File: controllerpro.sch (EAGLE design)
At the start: 11 parts

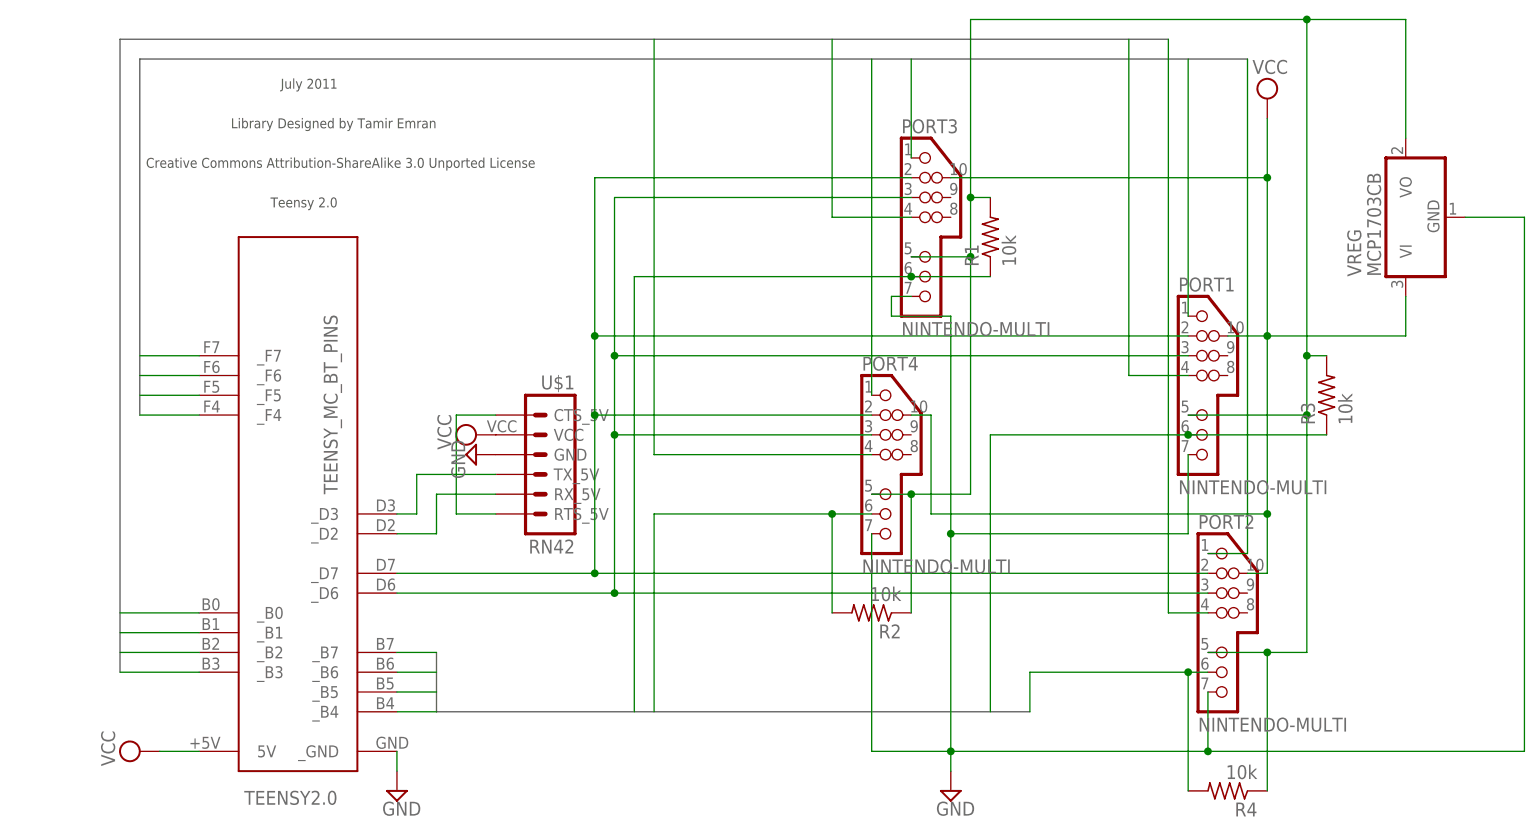
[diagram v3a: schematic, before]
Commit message: Switch VCC to 3.3v
Remove VREG, supply NES/SNES and N64 all with 3.3v
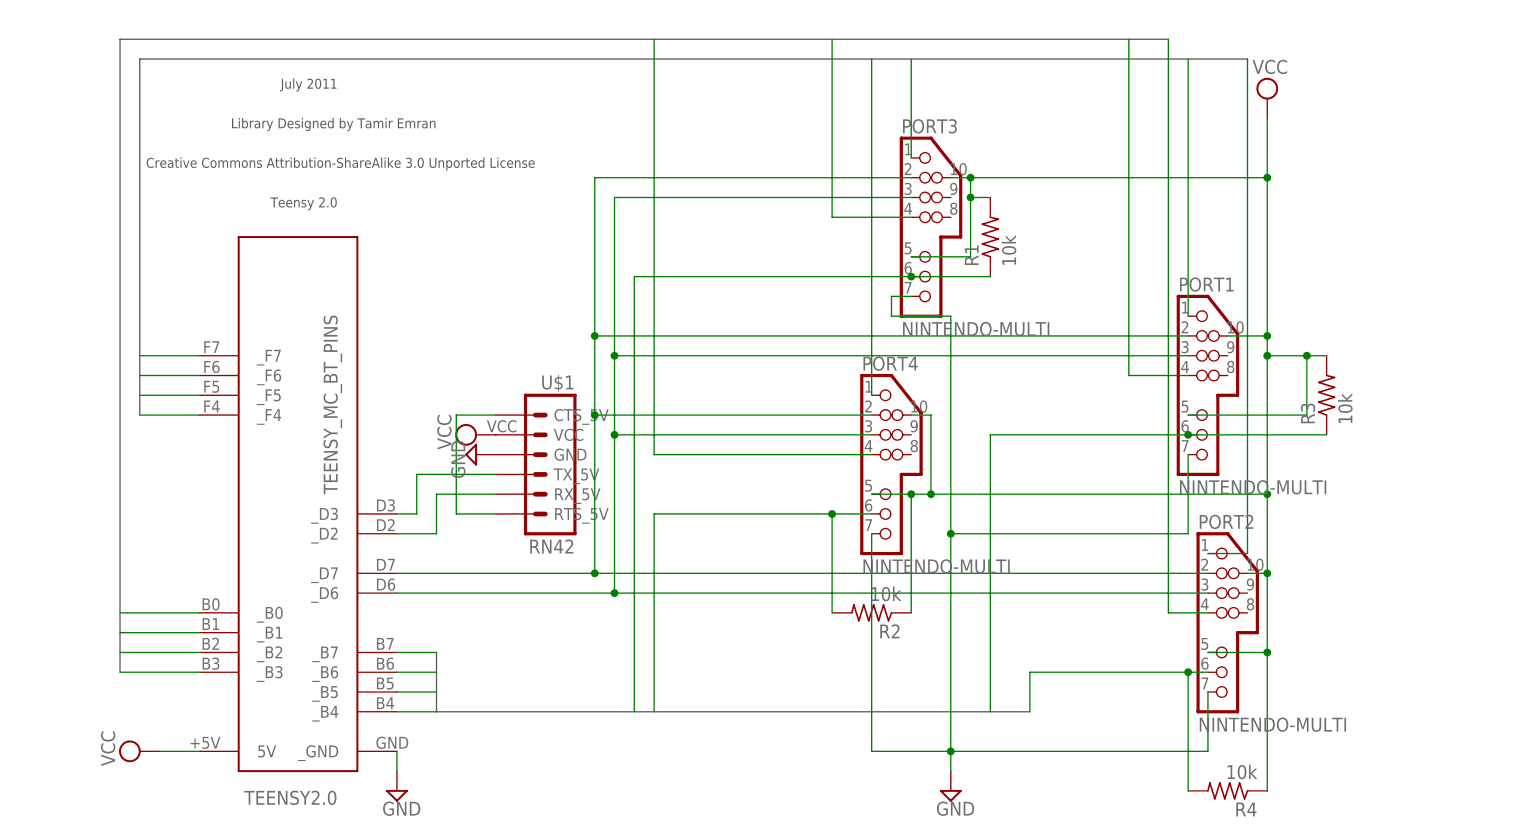
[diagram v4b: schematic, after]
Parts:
- removed VREG: MCP1703CB, linear:MCP1703CB
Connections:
- removed net V33: PORT1.5, PORT2.5, PORT3.5, PORT4.5, R1.2, R2.1, R3.2, R4.1, VREG.VO
- net GND: no longer VREG.GND
- net VCC: now also PORT1.5, PORT2.5, PORT3.5, PORT4.5, R1.2, R2.1, R3.2, R4.1; no longer VREG.VI
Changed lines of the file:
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@@
 <part name="SUPPLY2" library="supply2" deviceset="VCC" device=""/>
 <part name="SUPPLY3" library="supply2" deviceset="VCC" device=""/>
-<part name="VREG" library="linear" deviceset="MCP1703" device="CB"/>
 <part name="TEENSY2.0" library="custom" deviceset="TEENSY_MC_BT_PINS" device=""/>
 <part name="SUPPLY6" library="supply2" deviceset="GND" device=""/>
@@
 <instance part="SUPPLY2" gate="G$1" x="20.32" y="20.32" rot="R90"/>
 <instance part="SUPPLY3" gate="G$1" x="165.1" y="104.14"/>
-<instance part="VREG" gate="G$1" x="182.88" y="88.9" rot="R90"/>
 <instance part="TEENSY2.0" gate="G$1" x="40.64" y="53.34" rot="R180"/>
 <instance part="SUPPLY6" gate="GND" x="53.34" y="15.24"/>
@@
 <pinref part="PORT3" gate="G$1" pin="10"/>
 <pinref part="SUPPLY3" gate="G$1" pin="VCC"/>
-<wire x1="124.46" y1="93.98" x2="165.1" y2="93.98" width="0.1524" layer="91"/>
+<wire x1="124.46" y1="93.98" x2="127" y2="93.98" width="0.1524" layer="91"/>
+<wire x1="127" y1="93.98" x2="165.1" y2="93.98" width="0.1524" layer="91"/>
 <wire x1="165.1" y1="93.98" x2="165.1" y2="101.6" width="0.1524" layer="91"/>
 <pinref part="PORT2" gate="G$1" pin="10"/>
 <wire x1="162.56" y1="43.18" x2="165.1" y2="43.18" width="0.1524" layer="91"/>
-<wire x1="165.1" y1="43.18" x2="165.1" y2="50.8" width="0.1524" layer="91"/>
+<wire x1="165.1" y1="43.18" x2="165.1" y2="53.34" width="0.1524" layer="91"/>
 <pinref part="PORT1" gate="G$1" pin="10"/>
-<wire x1="165.1" y1="50.8" x2="165.1" y2="73.66" width="0.1524" layer="91"/>
+<wire x1="165.1" y1="53.34" x2="165.1" y2="71.12" width="0.1524" layer="91"/>
+<wire x1="165.1" y1="71.12" x2="165.1" y2="73.66" width="0.1524" layer="91"/>
 <wire x1="165.1" y1="73.66" x2="165.1" y2="93.98" width="0.1524" layer="91"/>
 <wire x1="160.02" y1="73.66" x2="165.1" y2="73.66" width="0.1524" layer="91"/>
 <pinref part="PORT4" gate="G$1" pin="10"/>
 <wire x1="119.38" y1="63.5" x2="121.92" y2="63.5" width="0.1524" layer="91"/>
-<wire x1="121.92" y1="63.5" x2="121.92" y2="50.8" width="0.1524" layer="91"/>
-<wire x1="121.92" y1="50.8" x2="165.1" y2="50.8" width="0.1524" layer="91"/>
-<junction x="165.1" y="50.8"/>
+<wire x1="121.92" y1="63.5" x2="121.92" y2="53.34" width="0.1524" layer="91"/>
+<wire x1="121.92" y1="53.34" x2="165.1" y2="53.34" width="0.1524" layer="91"/>
+<junction x="165.1" y="53.34"/>
 <junction x="165.1" y="73.66"/>
 <junction x="165.1" y="93.98"/>
-<wire x1="182.88" y1="73.66" x2="165.1" y2="73.66" width="0.1524" layer="91"/>
-<pinref part="VREG" gate="G$1" pin="VI"/>
-<wire x1="182.88" y1="73.66" x2="182.88" y2="78.74" width="0.1524" layer="91"/>
+<pinref part="PORT4" gate="G$1" pin="5"/>
+<wire x1="119.38" y1="53.34" x2="114.3" y2="53.34" width="0.1524" layer="91"/>
+<pinref part="R2" gate="G$1" pin="1"/>
+<wire x1="119.38" y1="38.1" x2="119.38" y2="53.34" width="0.1524" layer="91"/>
+<junction x="119.38" y="53.34"/>
+<wire x1="121.92" y1="53.34" x2="119.38" y2="53.34" width="0.1524" layer="91"/>
+<pinref part="PORT3" gate="G$1" pin="5"/>
+<wire x1="119.38" y1="83.82" x2="127" y2="83.82" width="0.1524" layer="91"/>
+<wire x1="127" y1="91.44" x2="127" y2="83.82" width="0.1524" layer="91"/>
+<pinref part="R1" gate="G$1" pin="2"/>
+<wire x1="129.54" y1="91.44" x2="127" y2="91.44" width="0.1524" layer="91"/>
+<wire x1="127" y1="91.44" x2="127" y2="93.98" width="0.1524" layer="91"/>
+<junction x="127" y="93.98"/>
+<junction x="127" y="91.44"/>
+<pinref part="PORT1" gate="G$1" pin="5"/>
+<pinref part="R3" gate="G$1" pin="2"/>
+<wire x1="172.72" y1="71.12" x2="170.18" y2="71.12" width="0.1524" layer="91"/>
+<wire x1="170.18" y1="71.12" x2="170.18" y2="63.5" width="0.1524" layer="91"/>
+<wire x1="170.18" y1="63.5" x2="154.94" y2="63.5" width="0.1524" layer="91"/>
+<junction x="170.18" y="71.12"/>
+<wire x1="170.18" y1="71.12" x2="165.1" y2="71.12" width="0.1524" layer="91"/>
+<junction x="165.1" y="71.12"/>
+<junction x="121.92" y="53.34"/>
+<pinref part="R4" gate="G$1" pin="1"/>
+<pinref part="PORT2" gate="G$1" pin="5"/>
+<wire x1="157.48" y1="33.02" x2="165.1" y2="33.02" width="0.1524" layer="91"/>
+<wire x1="165.1" y1="33.02" x2="165.1" y2="15.24" width="0.1524" layer="91"/>
+<wire x1="165.1" y1="43.18" x2="165.1" y2="33.02" width="0.1524" layer="91"/>
+<junction x="165.1" y="33.02"/>
+<junction x="165.1" y="43.18"/>
 </segment>
 <segment>
@@
 <junction x="124.46" y="20.32"/>
 <wire x1="124.46" y1="48.26" x2="124.46" y2="20.32" width="0.1524" layer="91"/>
-<wire x1="157.48" y1="20.32" x2="198.12" y2="20.32" width="0.1524" layer="91"/>
 <wire x1="124.46" y1="76.2" x2="116.84" y2="76.2" width="0.1524" layer="91"/>
 <wire x1="116.84" y1="76.2" x2="116.84" y2="78.74" width="0.1524" layer="91"/>
 <pinref part="PORT3" gate="G$1" pin="7"/>
 <wire x1="116.84" y1="78.74" x2="119.38" y2="78.74" width="0.1524" layer="91"/>
-<pinref part="VREG" gate="G$1" pin="GND"/>
-<wire x1="190.5" y1="88.9" x2="198.12" y2="88.9" width="0.1524" layer="91"/>
-<wire x1="198.12" y1="88.9" x2="198.12" y2="20.32" width="0.1524" layer="91"/>
 <pinref part="PORT1" gate="G$1" pin="7"/>
 <wire x1="154.94" y1="58.42" x2="154.94" y2="48.26" width="0.1524" layer="91"/>
 <wire x1="154.94" y1="48.26" x2="124.46" y2="48.26" width="0.1524" layer="91"/>
 <junction x="124.46" y="48.26"/>
-<junction x="157.48" y="20.32"/>
 </segment>
 <segment>
@@
 </segment>
 </net>
-<net name="V33" class="0">
-<segment>
-<wire x1="170.18" y1="114.3" x2="127" y2="114.3" width="0.1524" layer="91"/>
-<wire x1="127" y1="114.3" x2="127" y2="91.44" width="0.1524" layer="91"/>
-<pinref part="PORT4" gate="G$1" pin="5"/>
-<wire x1="127" y1="91.44" x2="127" y2="83.82" width="0.1524" layer="91"/>
-<wire x1="127" y1="83.82" x2="127" y2="53.34" width="0.1524" layer="91"/>
-<wire x1="127" y1="53.34" x2="119.38" y2="53.34" width="0.1524" layer="91"/>
-<pinref part="PORT3" gate="G$1" pin="5"/>
-<wire x1="119.38" y1="53.34" x2="114.3" y2="53.34" width="0.1524" layer="91"/>
-<wire x1="119.38" y1="83.82" x2="127" y2="83.82" width="0.1524" layer="91"/>
-<wire x1="170.18" y1="114.3" x2="170.18" y2="71.12" width="0.1524" layer="91"/>
-<pinref part="PORT1" gate="G$1" pin="5"/>
-<wire x1="170.18" y1="71.12" x2="170.18" y2="63.5" width="0.1524" layer="91"/>
-<wire x1="170.18" y1="63.5" x2="154.94" y2="63.5" width="0.1524" layer="91"/>
-<pinref part="PORT2" gate="G$1" pin="5"/>
-<wire x1="157.48" y1="33.02" x2="165.1" y2="33.02" width="0.1524" layer="91"/>
-<wire x1="165.1" y1="33.02" x2="170.18" y2="33.02" width="0.1524" layer="91"/>
-<wire x1="170.18" y1="33.02" x2="170.18" y2="63.5" width="0.1524" layer="91"/>
-<junction x="170.18" y="63.5"/>
-<junction x="127" y="83.82"/>
-<pinref part="VREG" gate="G$1" pin="VO"/>
-<wire x1="182.88" y1="99.06" x2="182.88" y2="114.3" width="0.1524" layer="91"/>
-<wire x1="182.88" y1="114.3" x2="170.18" y2="114.3" width="0.1524" layer="91"/>
-<junction x="170.18" y="114.3"/>
-<pinref part="R1" gate="G$1" pin="2"/>
-<wire x1="129.54" y1="91.44" x2="127" y2="91.44" width="0.1524" layer="91"/>
-<pinref part="R2" gate="G$1" pin="1"/>
-<wire x1="119.38" y1="38.1" x2="119.38" y2="53.34" width="0.1524" layer="91"/>
-<junction x="119.38" y="53.34"/>
-<junction x="127" y="91.44"/>
-<pinref part="R4" gate="G$1" pin="1"/>
-<wire x1="165.1" y1="33.02" x2="165.1" y2="15.24" width="0.1524" layer="91"/>
-<pinref part="R3" gate="G$1" pin="2"/>
-<wire x1="172.72" y1="71.12" x2="170.18" y2="71.12" width="0.1524" layer="91"/>
-<junction x="170.18" y="71.12"/>
-<junction x="165.1" y="33.02"/>
-</segment>
-</net>
